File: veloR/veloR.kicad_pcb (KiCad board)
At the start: 2 copper layers, 120.1 x 88.5 mm, 48 parts, among them J3 DISPLAY, J4 Conn_01x10, J9 Programador, M1 M1, M2 M2, M3 Motor_DC, M4 Motor_DC, SW1 SW_DPST_x2, SW10 SW_Push, U3 AMS1117-3.3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

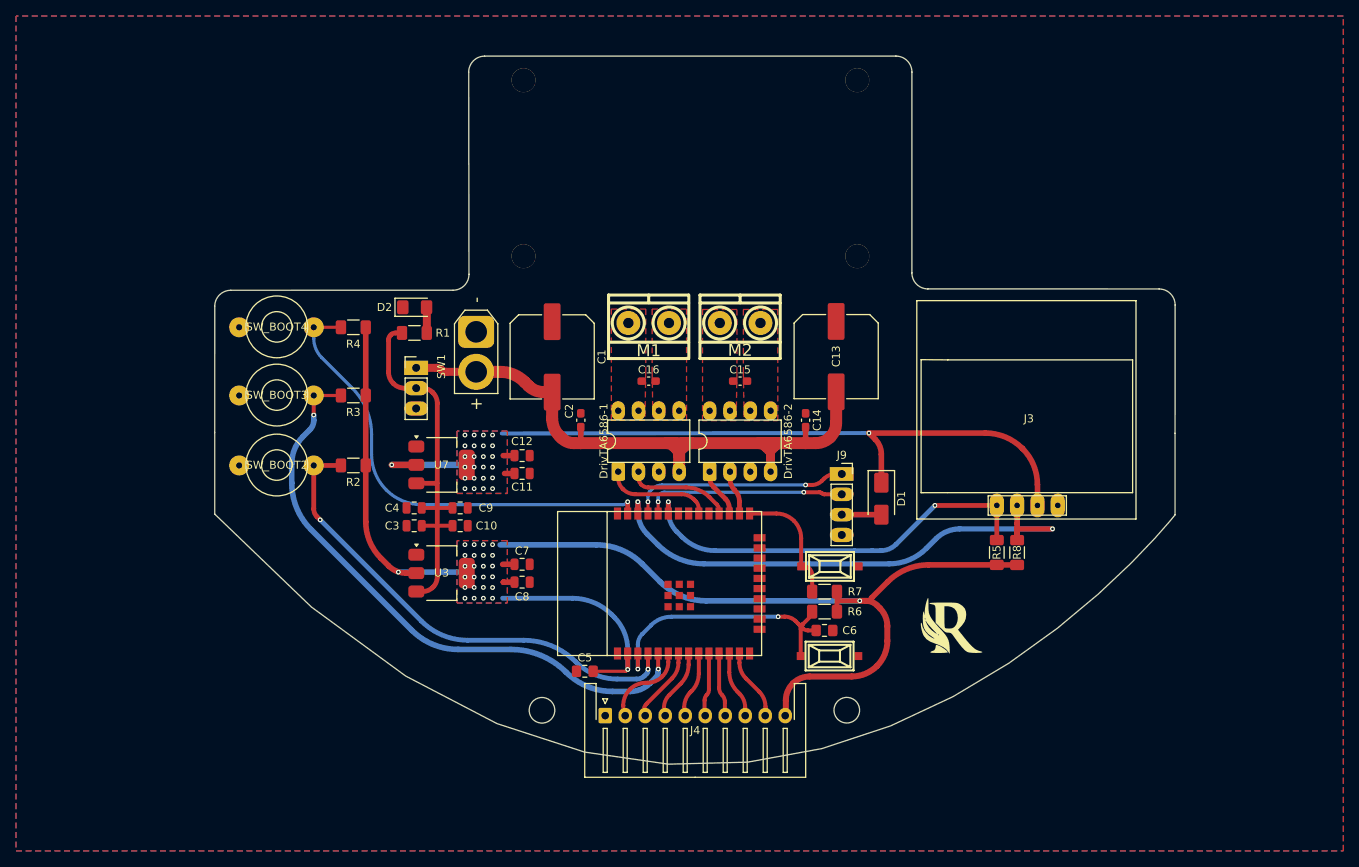
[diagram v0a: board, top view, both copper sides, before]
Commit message: Add files via upload
en este archivo se cambio los reguladores de tension por step down mini 360
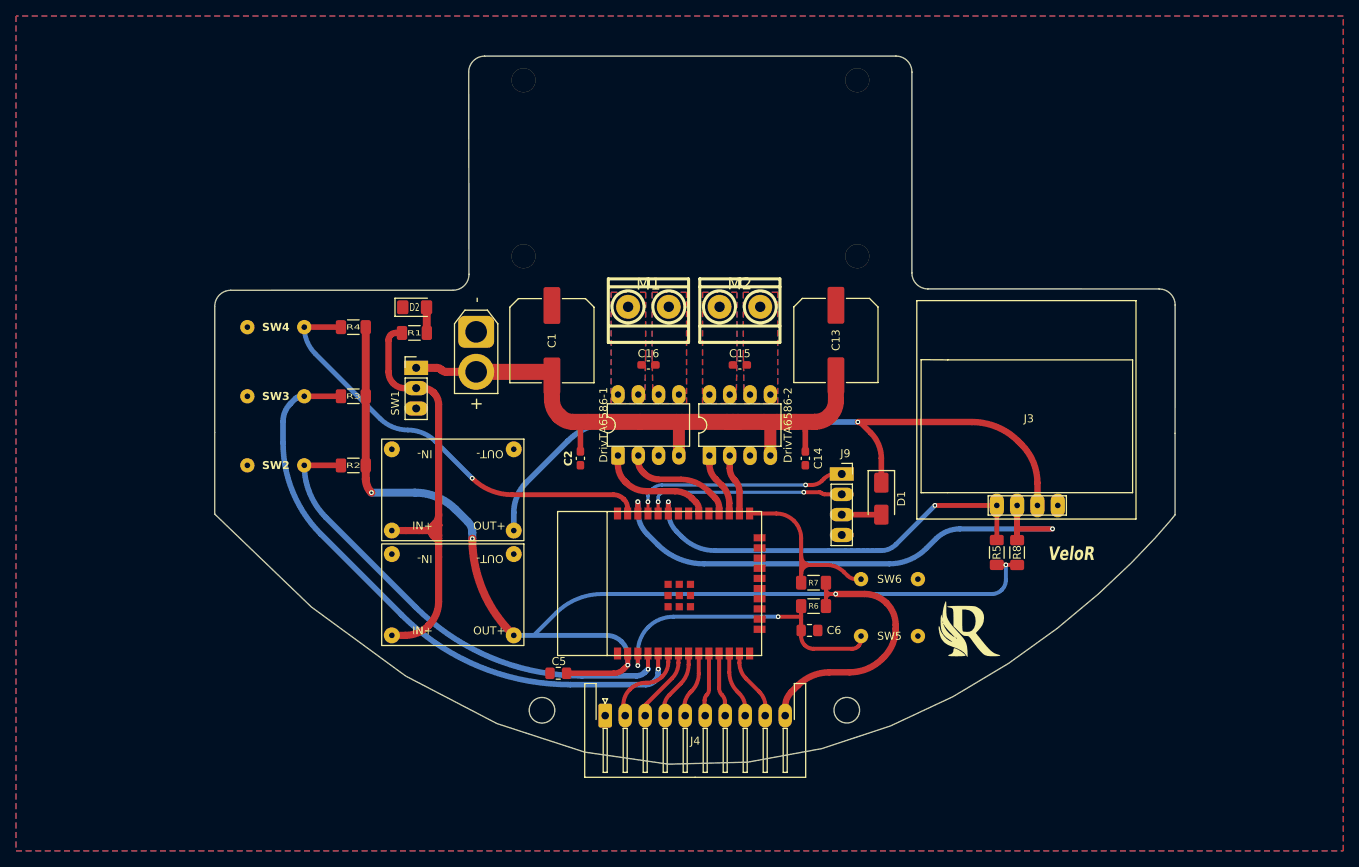
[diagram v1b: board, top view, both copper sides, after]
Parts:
- removed C10, C11, C4, C7: 100nF, Capacitor_SMD:C_0805_2012Metric
- removed C12, C3, C8, C9: 10uF, Capacitor_SMD:C_0805_2012Metric
- removed SW10, SW_BOOT1: SW_Push, EESTN5:Pulsador_SMD_2_ALTO
- removed SW_BOOT2, SW_BOOT3, SW_BOOT4: SW_Push, MacroLib:Button
- removed U3: AMS1117-3.3, Package_TO_SOT_SMD:SOT-223-3_TabPin2
- removed U7: AMS1117-5.0, Package_TO_SOT_SMD:SOT-223-3_TabPin2
- added G***: LOGO, LOGO, B.Cu at (186.6, 93.0)
- added SW2: SW_Push_Dual_x2, NUEVAS HUELLAS TREJO:SW 6MM 2 PIN, F.Cu at (92.2, 106.9)
- added SW3: SW_Push_Dual_x2, NUEVAS HUELLAS TREJO:SW 6MM 2 PIN, F.Cu at (92.2, 98.3)
- added SW4: SW_Push_Dual_x2, NUEVAS HUELLAS TREJO:SW 6MM 2 PIN, F.Cu at (92.2, 89.7)
- added SW5: SW_Push_Dual_x2, NUEVAS HUELLAS TREJO:SW 6MM 2 PIN, F.Cu at (169.4, 128.8)
- added SW6: SW_Push_Dual_x2, NUEVAS HUELLAS TREJO:SW 6MM 2 PIN, F.Cu at (169.4, 121.7)
- added U1: ~, NUEVAS HUELLAS TREJO:STEP DOWN MINI 360, F.Cu at (114.6, 123.4)
- added U2: ~, NUEVAS HUELLAS TREJO:STEP DOWN MINI 360, F.Cu at (114.6, 110.3)
- moved C2 4.77 mm to (130.5, 106.3), turned to 90 degrees
- moved C14 4.77 mm to (158.7, 106.3), turned to 90 degrees
- moved C5 3.33 mm to (127.8, 133.2)
- moved G*** 2.27 mm to (179.1, 127.5)
- moved C15 2.02 mm to (150.5, 94.6)
- moved C16 2.02 mm to (139.0, 94.6)
- moved DrivTA6586-1 2.02 mm to (135.2, 106.0)
- moved C1 2.02 mm to (127.0, 91.6)
- moved C13 2.02 mm to (162.5, 91.6)
- moved DrivTA6586-2 2.02 mm to (146.7, 106.0)
- moved M1 2.02 mm to (139.0, 87.4)
- moved M2 2.02 mm to (150.5, 87.4)
- moved C6 1.87 mm to (159.2, 127.8)
- moved R7 1.77 mm to (159.7, 121.9)
- moved R6 1.54 mm to (159.7, 124.8)
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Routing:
- net BT: track 15.7 -> 24.0 mm
- net VCC1: track 50.1 -> 57.9 mm
- net +5V: track 94.9 -> 88.6 mm, vias 26 -> 1
- net 3V3: track 171.5 -> 177.6 mm, vias 27 -> 5
- net VCC: track 81.7 -> 78.1 mm
- net SW3: track 58.8 -> 55.4 mm
- net EN: track 36.3 -> 39.5 mm
- net INA1: track 5.52 -> 7.55 mm
- net INB1: track 6.08 -> 8.00 mm
- net INA2: track 13.1 -> 14.3 mm
- net INB2: track 13.5 -> 14.6 mm
- net SW2: track 75.5 -> 76.1 mm, vias 2 -> 1
- net SW1: vias 2 -> 1
- added copper zone on B.Cu, net M1
- added copper zone on B.Cu, net M2
- added copper zone on B.Cu, net M3
- added copper zone on B.Cu, net M4
- removed copper zone on B.Cu, net +5V
- removed copper zone on F.Cu, net +5V
- removed copper zone on B.Cu, net 3V3
- removed copper zone on F.Cu, net 3V3
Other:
- board text added: "VeloR"
